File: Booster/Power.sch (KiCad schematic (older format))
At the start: 7 parts, among them J301 15VDC, Q301 FQP47P06, U301 LM78L05

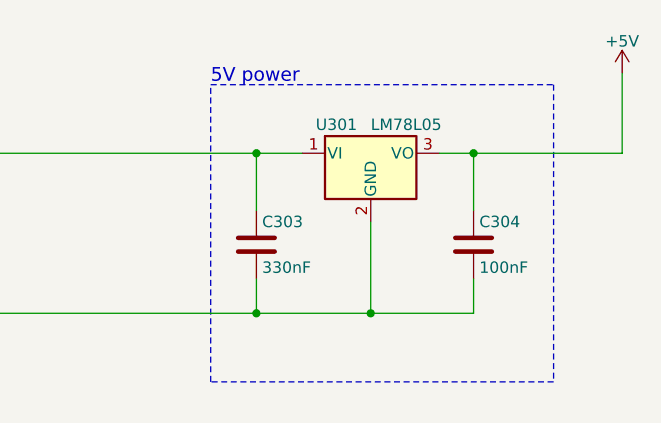
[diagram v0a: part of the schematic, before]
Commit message: Fixed 7805 ->7805
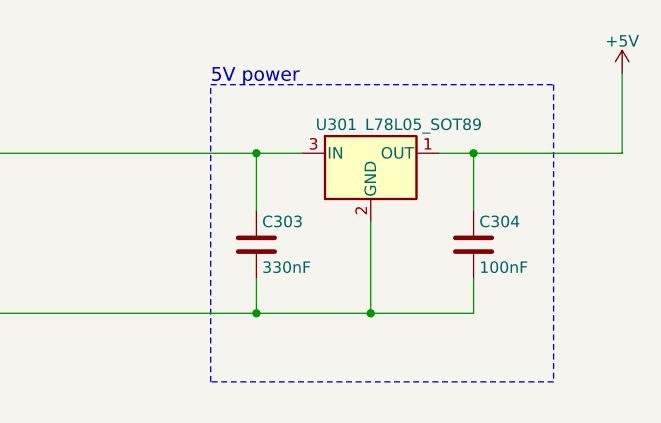
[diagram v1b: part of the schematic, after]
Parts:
- removed U301: LM78L05, TO_SOT_Packages_SMD:SOT-89-3, symbol LM7805_TO220
- added U301: L78L05_SOT89, TO_SOT_Packages_SMD:SOT-89-3, symbol L78L05_SOT89
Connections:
- net +15V: now also U301.3 (IN)
- net +5V: now also U301.1 (OUT)
- net GND: now also U301.2 (GND)
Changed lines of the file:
@@
 $EndDescr
-$Comp
-L LM7805_TO220 U301
-U 1 1 59E902F4
-P 7150 3400
-F 0 "U301" H 7000 3525 50  0000 C CNN
-F 1 "LM78L05" H 7150 3525 50  0000 L CNN
-F 2 "TO_SOT_Packages_SMD:SOT-89-3" H 7150 3625 50  0001 C CIN
-F 3 "" H 7150 3350 50  0001 C CNN
-	1    7150 3400
-	1    0    0    -1
-$EndComp
 $Comp
 L C C303
@@
 	3600 3700 3600 4100
 Connection ~ 3600 4100
+$Comp
+L L78L05_SOT89 U301
+U 1 1 5A7C2FD2
+P 7150 3400
+F 0 "U301" H 7000 3525 50  0000 C CNN
+F 1 "L78L05_SOT89" H 7125 3525 50  0000 L CNN
+F 2 "TO_SOT_Packages_SMD:SOT-89-3" H 7150 3600 50  0001 C CIN
+F 3 "" H 7150 3350 50  0001 C CNN
+	1    7150 3400
+	1    0    0    -1
+$EndComp
 $EndSCHEMATC
